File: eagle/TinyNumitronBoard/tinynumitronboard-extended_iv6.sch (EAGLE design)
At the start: 50 parts, among them IC1 74LS595D

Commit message: IV6 board dev continued.
Before taking some leap on placement. Schematics are ok minus final
review.
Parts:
- removed J1, J2: (no value), SparkFun-Connectors:M01NOSILK-KIT
- removed LED2, LED3, LED4: (no value), led:LEDKA-3528ASYC
- removed R10, R11, R12, R13, R14, R15, R16, R17, R18, R19, R20, R21, R22, R23, R24, R25, R26, R27, R28, R29, R30, R31, R32, R9: (no value), resistor:R-EU_R1206
- removed U$2, U$5, U$7: IV16TINY_NUMITRON, kalshagar:IV16TINY_NUMITRON
- removed UC2, UC3, UC4: 74HC595_SMDDIP_COMBOTHINPAD, kalshagar:74HC595_SMDDIP_COMBOTHINPAD
- added DRIVER2, DRIVER3, DRIVER4: ULN2803, uln2803:ULN2803
- added FILGND2GND: JUMPER-PAD-2-NOYES_SILK, SparkFun-Passives:JUMPER-PAD-2-NOYES_SILK
- added J_LED_IN, J_LED_OUT: (no value), SparkFun-Connectors:M01NOSILK-KIT
- added J_TUBEPOWER_IN, J_TUBEPOWER_OUT: (no value), SparkFun-Connectors:M03LOCK
- added SER2, SER3, SER4: 74LS595D, SparkFun-DigitalIC:74LS595D
- added TUBE2, TUBE3, TUBE4: IV6_NUMITRONLARGE, kalshagar:IV6_NUMITRONLARGE
- C1: device resistor:C-EU050-024X044 -> resistor:C-EUC1206
- renumbered IC1 to SER1, U$4 to TUBE1, U$6 to DRIVER1
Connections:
- removed net N$20: R9.2, U$2.BOTTOMLEFT
- removed net N$22: JP_OUTPUT.5, JP_OUTPUT.6, UC4.QH*
- removed net N$75: R31.1, UC3.QG
- removed net N$76: R32.1, UC3.QH
- removed net N$77: LED3.A, R32.2, U$7.DOT
- removed net N$78: UC3.QH*, UC4.SER
- new net FIL_M: FILGND2GND.1, J_TUBEPOWER_IN.3, J_TUBEPOWER_OUT.3, TUBE1.FIL_M, TUBE2.FIL_M, TUBE3.FIL_M, TUBE4.FIL_M
- new net FIL_P: J_TUBEPOWER_IN.2, J_TUBEPOWER_OUT.2, TUBE1.FIL_P, TUBE2.FIL_P, TUBE3.FIL_P, TUBE4.FIL_P
- new net GRID_P: J_TUBEPOWER_IN.1, J_TUBEPOWER_OUT.1, TUBE1.GRID_P, TUBE2.GRID_P, TUBE3.GRID_P, TUBE4.GRID_P
- new net N$13: SER2.QH*, SER3.SER
- new net N$14: DRIVER2.OUT1, TUBE2.BL
- new net N$16: DRIVER2.OUT2, TUBE2.BOTTOM
- new net N$17: DRIVER2.OUT3, TUBE2.MIDDLE
- new net N$60: DRIVER3.OUT3, TUBE3.MIDDLE
- new net N$61: DRIVER3.OUT4, TUBE3.TL
- net GND: now also DRIVER2.GND, DRIVER3.GND, DRIVER4.GND, FILGND2GND.2, SER2.G, SER2.GND, SER3.G, SER3.GND, SER4.G, SER4.GND; no longer LED2.C, LED3.C, LED4.C, UC2.G, UC2.GND, UC3.G, UC3.GND, UC4.G, UC4.GND
- net N$12: now also J_LED_IN.1; no longer J1.1
- net N$21: now also JP_OUTPUT.5, JP_OUTPUT.6, SER4.QH*; no longer R10.2, U$2.BOTTOM
- net N$23: now also SER2.SER; no longer UC2.SER
- net N$24: now also DRIVER4.OUT1, TUBE4.BL; no longer R11.2, U$2.MIDDLE
- net N$25: now also DRIVER4.OUT2, TUBE4.BOTTOM; no longer R12.2, U$2.TOPLEFT
- net N$26: now also DRIVER4.OUT3, TUBE4.MIDDLE; no longer R13.2, U$2.TOP
- net N$27: now also DRIVER4.OUT4, TUBE4.TL; no longer R14.2, U$2.BOTTOMRIGHT
- net N$28: now also DRIVER4.OUT5, TUBE4.TOP; no longer R15.2, U$2.TOPRIGHT
- net N$29: now also DRIVER4.OUT6, TUBE4.BR; no longer R9.1, UC4.QA
- net N$30: now also DRIVER4.OUT7, TUBE4.TR; no longer R10.1, UC4.QB
- net N$31: now also DRIVER4.OUT8, TUBE4.DOT; no longer R11.1, UC4.QC
- net N$32: now also DRIVER4.IN1, SER4.QA; no longer R12.1, UC4.QD
- net N$33: now also DRIVER4.IN2, SER4.QB; no longer R13.1, UC4.QE
- net N$34: now also DRIVER4.IN3, SER4.QC; no longer R14.1, UC4.QF
- net N$35: now also DRIVER4.IN4, SER4.QD; no longer R15.1, UC4.QG
- net N$36: now also DRIVER4.IN5, SER4.QE; no longer R16.1, UC4.QH
- net N$37: now also DRIVER4.IN6, SER4.QF; no longer LED4.A, R16.2, U$2.DOT
- net N$39: now also DRIVER2.OUT4, TUBE2.TL; no longer R17.2, U$5.BOTTOMLEFT
- net N$40: now also DRIVER2.OUT5, TUBE2.TOP; no longer R18.2, U$5.BOTTOM
- net N$41: now also DRIVER2.OUT6, TUBE2.BR; no longer R19.2, U$5.MIDDLE
- net N$42: now also DRIVER2.OUT7, TUBE2.TR; no longer R20.2, U$5.TOPLEFT
- net N$43: now also DRIVER2.OUT8, TUBE2.DOT; no longer R21.2, U$5.TOP
- net N$44: now also DRIVER2.IN1, SER2.QA; no longer R22.2, U$5.BOTTOMRIGHT
- net N$45: now also DRIVER2.IN2, SER2.QB; no longer R23.2, U$5.TOPRIGHT
- net N$46: now also DRIVER2.IN3, SER2.QC; no longer R17.1, UC2.QA
- net N$47: now also DRIVER2.IN4, SER2.QD; no longer R18.1, UC2.QB
- net N$48: now also DRIVER2.IN5, SER2.QE; no longer R19.1, UC2.QC
- net N$49: now also DRIVER2.IN6, SER2.QF; no longer R20.1, UC2.QD
- net N$50: now also DRIVER2.IN7, SER2.QG; no longer R21.1, UC2.QE
- net N$51: now also DRIVER2.IN8, SER2.QH; no longer R22.1, UC2.QF
- net N$52: now also DRIVER4.IN7, SER4.QG; no longer R23.1, UC2.QG
- net N$53: now also SER3.QH*, SER4.SER; no longer R24.1, UC2.QH
- net N$54: now also DRIVER3.OUT1, TUBE3.BL; no longer LED2.A, R24.2, U$5.DOT
- net N$58: now also DRIVER3.OUT2, TUBE3.BOTTOM; no longer UC2.QH*, UC3.SER
- net N$62: now also DRIVER3.OUT5, TUBE3.TOP; no longer R25.2, U$7.BOTTOMLEFT
- net N$63: now also DRIVER3.OUT6, TUBE3.BR; no longer R26.2, U$7.BOTTOM
- net N$64: now also DRIVER3.OUT7, TUBE3.TR; no longer R27.2, U$7.MIDDLE
- net N$65: now also DRIVER3.OUT8, TUBE3.DOT; no longer R28.2, U$7.TOPLEFT
- net N$66: now also DRIVER3.IN1, SER3.QA; no longer R29.2, U$7.TOP
- net N$67: now also DRIVER3.IN2, SER3.QB; no longer R30.2, U$7.BOTTOMRIGHT
- net N$68: now also DRIVER3.IN3, SER3.QC; no longer R31.2, U$7.TOPRIGHT
- net N$69: now also DRIVER3.IN4, SER3.QD; no longer R25.1, UC3.QA
- net N$70: now also DRIVER3.IN5, SER3.QE; no longer R26.1, UC3.QB
- net N$71: now also DRIVER3.IN6, SER3.QF; no longer R27.1, UC3.QC
- net N$72: now also DRIVER3.IN7, SER3.QG; no longer R28.1, UC3.QD
- net N$73: now also DRIVER3.IN8, SER3.QH; no longer R29.1, UC3.QE
- net N$74: now also DRIVER4.IN8, SER4.QH; no longer R30.1, UC3.QF
- net RCK: now also SER2.RCK, SER3.RCK, SER4.RCK; no longer UC2.RCK, UC3.RCK, UC4.RCK
- net SCK: now also SER2.SCK, SER3.SCK, SER4.SCK; no longer UC2.SCK, UC3.SCK, UC4.SCK
- net VCC: now also J_LED_OUT.1, SER2.SCL, SER2.VCC, SER3.SCL, SER3.VCC, SER4.SCL, SER4.VCC; no longer J2.1, U$2.VCC, U$5.VCC, U$7.VCC, UC2.SCL, UC2.VCC, UC3.SCL, UC3.VCC, UC4.SCL, UC4.VCC
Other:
- moved on the sheet: C2, D1, D2, D3, D4

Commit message: Layout first draft finished.
Todo review.
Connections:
- new net N$20: D4.DOUT, J_LED_OUT.1
- net VCC: no longer J_LED_OUT.1
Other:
- moved on the sheet: C2, J_LED_OUT
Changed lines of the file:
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@@
 <part name="J_LED_IN" library="SparkFun-Connectors" deviceset="M01" device="NOSILK-KIT"/>
 <part name="J_LED_OUT" library="SparkFun-Connectors" deviceset="M01" device="NOSILK-KIT"/>
-<part name="C2" library="SparkFun-Passives" deviceset="CAP_POL" device="D"/>
 <part name="TUBE2" library="kalshagar" deviceset="IV6_NUMITRON" device="LARGE" value="IV6_NUMITRONLARGE"/>
 <part name="DRIVER2" library="uln2803" deviceset="ULN2803" device=""/>
@@
 <part name="J_TUBEPOWER_OUT" library="SparkFun-Connectors" deviceset="M03" device="LOCK"/>
 <part name="FILGND2GND" library="SparkFun-Passives" deviceset="JUMPER-PAD-2-NO" device="YES_SILK"/>
+<part name="C2" library="SparkFun-Passives" deviceset="CAP_POL" device="D"/>
 </parts>
 <sheets>
@@
 <instance part="D4" gate="G$1" x="-15.24" y="111.76"/>
 <instance part="J_LED_IN" gate="G$1" x="109.22" y="116.84" rot="R180"/>
-<instance part="J_LED_OUT" gate="G$1" x="-40.64" y="116.84"/>
-<instance part="C2" gate="G$1" x="-25.4" y="106.68"/>
+<instance part="J_LED_OUT" gate="G$1" x="-45.72" y="109.22"/>
 <instance part="TUBE2" gate="G$1" x="71.12" y="7.62" rot="R180"/>
 <instance part="DRIVER2" gate="G$1" x="5.08" y="0"/>
@@
 <instance part="J_TUBEPOWER_OUT" gate="J$1" x="114.3" y="-144.78" rot="R270"/>
 <instance part="FILGND2GND" gate="G$1" x="124.46" y="60.96"/>
+<instance part="C2" gate="G$1" x="-119.38" y="45.72"/>
 </instances>
 <busses>
@@
 <segment>
 <pinref part="JP_INPUT" gate="G$1" pin="2"/>
-<wire x1="-124.46" y1="55.88" x2="-91.44" y2="55.88" width="0.1524" layer="91"/>
+<wire x1="-124.46" y1="55.88" x2="-119.38" y2="55.88" width="0.1524" layer="91"/>
+<wire x1="-119.38" y1="55.88" x2="-91.44" y2="55.88" width="0.1524" layer="91"/>
 <wire x1="-91.44" y1="55.88" x2="-91.44" y2="48.26" width="0.1524" layer="91"/>
+<pinref part="C2" gate="G$1" pin="+"/>
+<wire x1="-119.38" y1="48.26" x2="-119.38" y2="55.88" width="0.1524" layer="91"/>
+<junction x="-119.38" y="55.88"/>
 </segment>
 <segment>
@@
 </segment>
 <segment>
-<pinref part="D4" gate="G$1" pin="VDD"/>
 <wire x1="-20.32" y1="129.54" x2="-20.32" y2="124.46" width="0.1524" layer="91"/>
 <pinref part="D3" gate="G$1" pin="VDD"/>
-<wire x1="-20.32" y1="124.46" x2="-33.02" y2="116.84" width="0.1524" layer="91"/>
 <wire x1="-20.32" y1="124.46" x2="10.16" y2="124.46" width="0.1524" layer="91"/>
 <wire x1="10.16" y1="124.46" x2="10.16" y2="116.84" width="0.1524" layer="91"/>
@@
 <wire x1="71.12" y1="124.46" x2="71.12" y2="116.84" width="0.1524" layer="91"/>
 <label x="-20.32" y="129.54" size="1.778" layer="95"/>
-<pinref part="J_LED_OUT" gate="G$1" pin="1"/>
-<junction x="-33.02" y="116.84"/>
-<pinref part="C2" gate="G$1" pin="+"/>
-<wire x1="-25.4" y1="109.22" x2="-25.4" y2="111.76" width="0.1524" layer="91"/>
-<wire x1="-25.4" y1="111.76" x2="-33.02" y2="116.84" width="0.1524" layer="91"/>
-<wire x1="-33.02" y1="116.84" x2="-20.32" y2="116.84" width="0.1524" layer="91"/>
+<pinref part="D4" gate="G$1" pin="VDD"/>
+<wire x1="-20.32" y1="116.84" x2="-20.32" y2="124.46" width="0.1524" layer="91"/>
 </segment>
 <segment>
@@
 <segment>
 <pinref part="JP_INPUT" gate="G$1" pin="1"/>
-<wire x1="-124.46" y1="53.34" x2="-93.98" y2="53.34" width="0.1524" layer="91"/>
+<wire x1="-124.46" y1="53.34" x2="-111.76" y2="53.34" width="0.1524" layer="91"/>
+<wire x1="-111.76" y1="53.34" x2="-93.98" y2="53.34" width="0.1524" layer="91"/>
 <wire x1="-93.98" y1="53.34" x2="-93.98" y2="48.26" width="0.1524" layer="91"/>
+<pinref part="C2" gate="G$1" pin="-"/>
+<wire x1="-119.38" y1="40.64" x2="-111.76" y2="40.64" width="0.1524" layer="91"/>
+<wire x1="-111.76" y1="40.64" x2="-111.76" y2="53.34" width="0.1524" layer="91"/>
+<junction x="-111.76" y="53.34"/>
 </segment>
 <segment>
@@
 <wire x1="93.98" y1="101.6" x2="93.98" y2="109.22" width="0.1524" layer="91"/>
 <label x="96.52" y="101.6" size="1.778" layer="95"/>
-<pinref part="C2" gate="G$1" pin="-"/>
-<wire x1="-25.4" y1="101.6" x2="2.54" y2="101.6" width="0.1524" layer="91"/>
 </segment>
 <segment>
@@
 </segment>
 </net>
+<net name="N$20" class="0">
+<segment>
+<pinref part="J_LED_OUT" gate="G$1" pin="1"/>
+<wire x1="-20.32" y1="109.22" x2="-38.1" y2="109.22" width="0.1524" layer="91"/>
+<pinref part="D4" gate="G$1" pin="DOUT"/>
+</segment>
+</net>

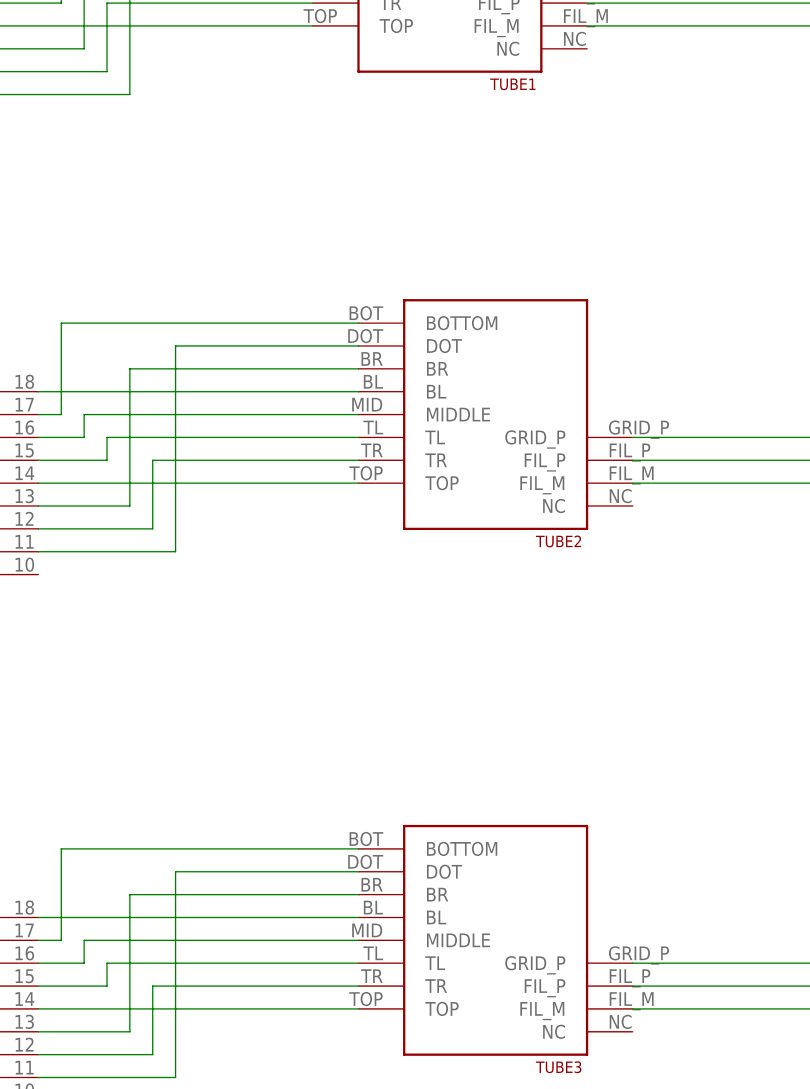
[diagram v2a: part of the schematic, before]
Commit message: Added options for 2 led in the middle
And a solder jumper for the dot or not (default not)
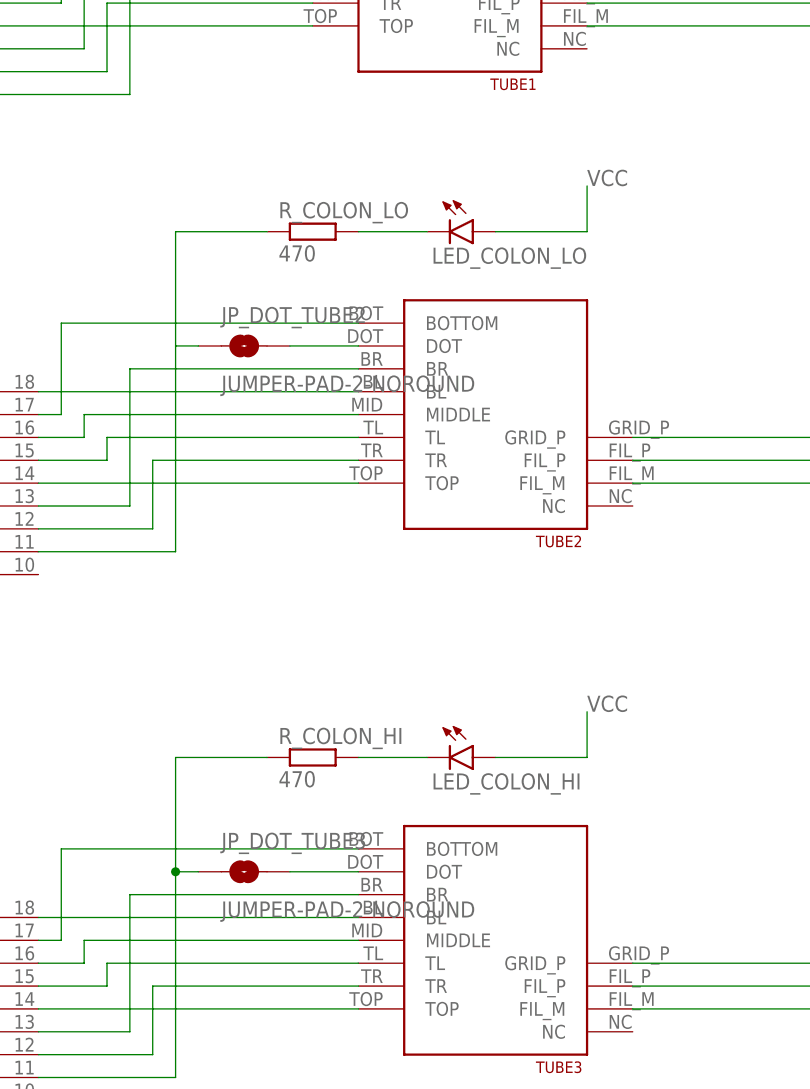
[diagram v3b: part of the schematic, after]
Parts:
- added JP_DOT_TUBE2, JP_DOT_TUBE3: JUMPER-PAD-2-NOROUND, SparkFun-Passives:JUMPER-PAD-2-NOROUND
- added LED_COLON_HI, LED_COLON_LO: (no value), SparkFun-LED:LED1206
- added R_COLON_HI, R_COLON_LO: 470, resistor:R-EU_M1206
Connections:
- new net N$22: LED_COLON_LO.C, R_COLON_LO.2
- new net N$75: JP_DOT_TUBE2.2, TUBE2.DOT
- new net N$76: JP_DOT_TUBE3.2, TUBE3.DOT
- new net N$77: LED_COLON_HI.C, R_COLON_HI.2
- net N$43: now also JP_DOT_TUBE2.1, R_COLON_LO.1; no longer TUBE2.DOT
- net N$65: now also JP_DOT_TUBE3.1, R_COLON_HI.1; no longer TUBE3.DOT
- net VCC: now also LED_COLON_HI.A, LED_COLON_LO.A
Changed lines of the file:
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@@
 <part name="FILGND2GND" library="SparkFun-Passives" deviceset="JUMPER-PAD-2-NO" device="YES_SILK"/>
 <part name="C2" library="SparkFun-Passives" deviceset="CAP_POL" device="D"/>
+<part name="LED_COLON_LO" library="SparkFun-LED" deviceset="LED" device="1206"/>
+<part name="R_COLON_LO" library="resistor" deviceset="R-EU_" device="M1206" value="470"/>
+<part name="JP_DOT_TUBE2" library="SparkFun-Passives" deviceset="JUMPER-PAD-2-NO" device="ROUND"/>
+<part name="LED_COLON_HI" library="SparkFun-LED" deviceset="LED" device="1206"/>
+<part name="R_COLON_HI" library="resistor" deviceset="R-EU_" device="M1206" value="470"/>
+<part name="JP_DOT_TUBE3" library="SparkFun-Passives" deviceset="JUMPER-PAD-2-NO" device="ROUND"/>
 </parts>
 <sheets>
@@
 <instance part="FILGND2GND" gate="G$1" x="124.46" y="60.96"/>
 <instance part="C2" gate="G$1" x="-119.38" y="45.72"/>
+<instance part="LED_COLON_LO" gate="G$1" x="68.58" y="27.94" rot="R270"/>
+<instance part="R_COLON_LO" gate="G$1" x="50.8" y="27.94"/>
+<instance part="JP_DOT_TUBE2" gate="G$1" x="43.18" y="15.24"/>
+<instance part="LED_COLON_HI" gate="G$1" x="68.58" y="-30.48" rot="R270"/>
+<instance part="R_COLON_HI" gate="G$1" x="50.8" y="-30.48"/>
+<instance part="JP_DOT_TUBE3" gate="G$1" x="43.18" y="-43.18"/>
 </instances>
 <busses>
@@
 <pinref part="SER4" gate="A" pin="SCL"/>
 </segment>
+<segment>
+<pinref part="LED_COLON_LO" gate="G$1" pin="A"/>
+<wire x1="71.12" y1="27.94" x2="81.28" y2="27.94" width="0.1524" layer="91"/>
+<wire x1="81.28" y1="27.94" x2="81.28" y2="33.02" width="0.1524" layer="91"/>
+<label x="81.28" y="33.02" size="1.778" layer="95"/>
+</segment>
+<segment>
+<pinref part="LED_COLON_HI" gate="G$1" pin="A"/>
+<wire x1="71.12" y1="-30.48" x2="81.28" y2="-30.48" width="0.1524" layer="91"/>
+<wire x1="81.28" y1="-30.48" x2="81.28" y2="-25.4" width="0.1524" layer="91"/>
+<label x="81.28" y="-25.4" size="1.778" layer="95"/>
+</segment>
 </net>
 <net name="GND" class="0">
@@
 <wire x1="20.32" y1="-7.62" x2="35.56" y2="-7.62" width="0.1524" layer="91"/>
 <wire x1="35.56" y1="-7.62" x2="35.56" y2="15.24" width="0.1524" layer="91"/>
-<pinref part="TUBE2" gate="G$1" pin="DOT"/>
-<wire x1="35.56" y1="15.24" x2="55.88" y2="15.24" width="0.1524" layer="91"/>
+<pinref part="R_COLON_LO" gate="G$1" pin="1"/>
+<wire x1="35.56" y1="15.24" x2="35.56" y2="27.94" width="0.1524" layer="91"/>
+<wire x1="45.72" y1="27.94" x2="35.56" y2="27.94" width="0.1524" layer="91"/>
+<pinref part="JP_DOT_TUBE2" gate="G$1" pin="1"/>
+<wire x1="38.1" y1="15.24" x2="35.56" y2="15.24" width="0.1524" layer="91"/>
 </segment>
 </net>
@@
 <wire x1="20.32" y1="-66.04" x2="35.56" y2="-66.04" width="0.1524" layer="91"/>
 <wire x1="35.56" y1="-66.04" x2="35.56" y2="-43.18" width="0.1524" layer="91"/>
-<pinref part="TUBE3" gate="G$1" pin="DOT"/>
-<wire x1="35.56" y1="-43.18" x2="55.88" y2="-43.18" width="0.1524" layer="91"/>
+<pinref part="R_COLON_HI" gate="G$1" pin="1"/>
+<wire x1="35.56" y1="-43.18" x2="35.56" y2="-30.48" width="0.1524" layer="91"/>
+<wire x1="45.72" y1="-30.48" x2="35.56" y2="-30.48" width="0.1524" layer="91"/>
+<pinref part="JP_DOT_TUBE3" gate="G$1" pin="1"/>
+<wire x1="38.1" y1="-43.18" x2="35.56" y2="-43.18" width="0.1524" layer="91"/>
+<junction x="35.56" y="-43.18"/>
 </segment>
 </net>
@@
 </segment>
 </net>
+<net name="N$22" class="0">
+<segment>
+<pinref part="R_COLON_LO" gate="G$1" pin="2"/>
+<pinref part="LED_COLON_LO" gate="G$1" pin="C"/>
+<wire x1="55.88" y1="27.94" x2="63.5" y2="27.94" width="0.1524" layer="91"/>
+</segment>
+</net>
+<net name="N$75" class="0">
+<segment>
+<pinref part="JP_DOT_TUBE2" gate="G$1" pin="2"/>
+<pinref part="TUBE2" gate="G$1" pin="DOT"/>
+<wire x1="48.26" y1="15.24" x2="55.88" y2="15.24" width="0.1524" layer="91"/>
+</segment>
+</net>
+<net name="N$77" class="0">
+<segment>
+<pinref part="R_COLON_HI" gate="G$1" pin="2"/>
+<pinref part="LED_COLON_HI" gate="G$1" pin="C"/>
+<wire x1="55.88" y1="-30.48" x2="63.5" y2="-30.48" width="0.1524" layer="91"/>
+</segment>
+</net>
+<net name="N$76" class="0">
+<segment>
+<pinref part="JP_DOT_TUBE3" gate="G$1" pin="2"/>
+<pinref part="TUBE3" gate="G$1" pin="DOT"/>
+<wire x1="48.26" y1="-43.18" x2="55.88" y2="-43.18" width="0.1524" layer="91"/>
+</segment>
+</net>
